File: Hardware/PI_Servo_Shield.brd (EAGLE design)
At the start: 65 x 30 mm, 89 parts, among them J1 RASPBERRYPI-40-PIN-GPIO, J19 QWIIC, J20 USB C, J21 Serial, U1 PCA9685, U2 PCA9306, U3 CH340C

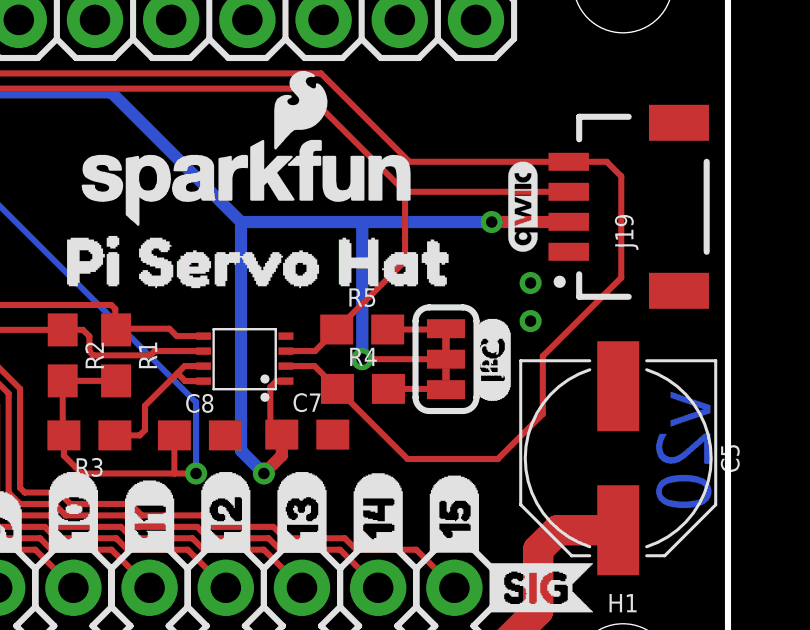
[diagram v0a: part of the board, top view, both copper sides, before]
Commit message: adjusted I2C pullup and label
modified sch note for bypass fuse jumper
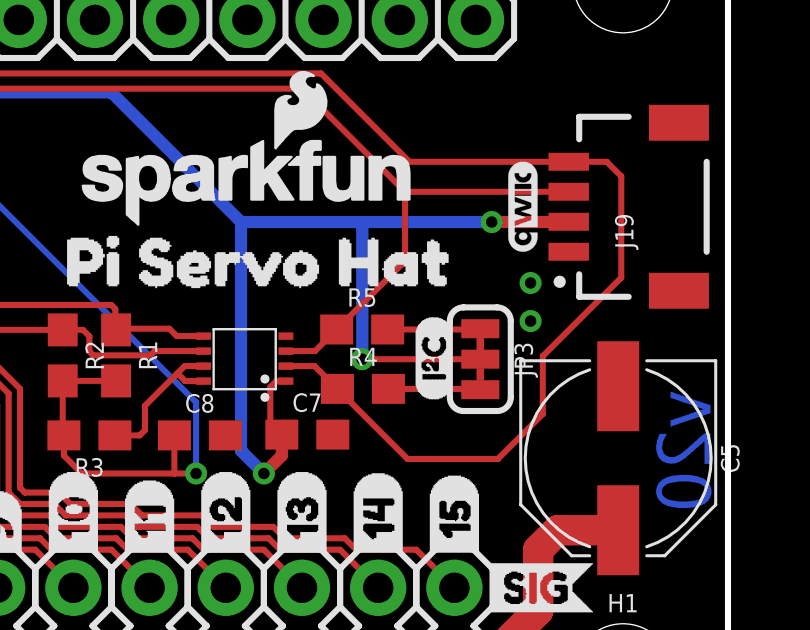
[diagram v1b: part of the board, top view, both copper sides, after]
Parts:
- moved U$2 1.96 mm to (55.2, 12.6)
- moved JP3 1.14 mm to (56.7, 14.0)
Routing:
- net N$2: track 1.93 -> 3.07 mm
- net 3.3VB: track 53.8 -> 54.9 mm
- net N$5: track 1.95 -> 3.10 mm
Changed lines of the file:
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@@
 <layer number="23" name="tOrigins" color="15" fill="1" visible="yes" active="yes"/>
 <layer number="24" name="bOrigins" color="15" fill="1" visible="yes" active="yes"/>
-<layer number="25" name="tNames" color="7" fill="1" visible="yes" active="yes"/>
-<layer number="26" name="bNames" color="7" fill="1" visible="yes" active="yes"/>
-<layer number="27" name="tValues" color="7" fill="1" visible="yes" active="yes"/>
-<layer number="28" name="bValues" color="7" fill="1" visible="yes" active="yes"/>
-<layer number="29" name="tStop" color="7" fill="3" visible="yes" active="yes"/>
-<layer number="30" name="bStop" color="7" fill="6" visible="yes" active="yes"/>
-<layer number="31" name="tCream" color="7" fill="4" visible="yes" active="yes"/>
-<layer number="32" name="bCream" color="7" fill="5" visible="yes" active="yes"/>
-<layer number="33" name="tFinish" color="6" fill="3" visible="yes" active="yes"/>
-<layer number="34" name="bFinish" color="6" fill="6" visible="yes" active="yes"/>
-<layer number="35" name="tGlue" color="7" fill="4" visible="yes" active="yes"/>
-<layer number="36" name="bGlue" color="7" fill="5" visible="yes" active="yes"/>
-<layer number="37" name="tTest" color="7" fill="1" visible="yes" active="yes"/>
-<layer number="38" name="bTest" color="7" fill="1" visible="yes" active="yes"/>
-<layer number="39" name="tKeepout" color="4" fill="11" visible="yes" active="yes"/>
-<layer number="40" name="bKeepout" color="1" fill="11" visible="yes" active="yes"/>
-<layer number="41" name="tRestrict" color="4" fill="10" visible="yes" active="yes"/>
-<layer number="42" name="bRestrict" color="1" fill="10" visible="yes" active="yes"/>
-<layer number="43" name="vRestrict" color="2" fill="10" visible="yes" active="yes"/>
-<layer number="44" name="Drills" color="7" fill="1" visible="yes" active="yes"/>
+<layer number="25" name="tNames" color="7" fill="1" visible="no" active="yes"/>
+<layer number="26" name="bNames" color="7" fill="1" visible="no" active="yes"/>
+<layer number="27" name="tValues" color="7" fill="1" visible="no" active="yes"/>
+<layer number="28" name="bValues" color="7" fill="1" visible="no" active="yes"/>
+<layer number="29" name="tStop" color="7" fill="3" visible="no" active="yes"/>
+<layer number="30" name="bStop" color="7" fill="6" visible="no" active="yes"/>
+<layer number="31" name="tCream" color="7" fill="4" visible="no" active="yes"/>
+<layer number="32" name="bCream" color="7" fill="5" visible="no" active="yes"/>
+<layer number="33" name="tFinish" color="6" fill="3" visible="no" active="yes"/>
+<layer number="34" name="bFinish" color="6" fill="6" visible="no" active="yes"/>
+<layer number="35" name="tGlue" color="7" fill="4" visible="no" active="yes"/>
+<layer number="36" name="bGlue" color="7" fill="5" visible="no" active="yes"/>
+<layer number="37" name="tTest" color="7" fill="1" visible="no" active="yes"/>
+<layer number="38" name="bTest" color="7" fill="1" visible="no" active="yes"/>
+<layer number="39" name="tKeepout" color="4" fill="11" visible="no" active="yes"/>
+<layer number="40" name="bKeepout" color="1" fill="11" visible="no" active="yes"/>
+<layer number="41" name="tRestrict" color="4" fill="10" visible="no" active="yes"/>
+<layer number="42" name="bRestrict" color="1" fill="10" visible="no" active="yes"/>
+<layer number="43" name="vRestrict" color="2" fill="10" visible="no" active="yes"/>
+<layer number="44" name="Drills" color="7" fill="1" visible="no" active="yes"/>
 <layer number="45" name="Holes" color="7" fill="1" visible="yes" active="yes"/>
-<layer number="46" name="Milling" color="3" fill="1" visible="yes" active="yes"/>
-<layer number="47" name="Measures" color="7" fill="1" visible="yes" active="yes"/>
-<layer number="48" name="Document" color="7" fill="1" visible="yes" active="yes"/>
+<layer number="46" name="Milling" color="3" fill="1" visible="no" active="yes"/>
+<layer number="47" name="Measures" color="7" fill="1" visible="no" active="yes"/>
+<layer number="48" name="Document" color="7" fill="1" visible="no" active="yes"/>
 <layer number="49" name="Reference" color="7" fill="1" visible="yes" active="yes"/>
-<layer number="50" name="dxf" color="7" fill="1" visible="yes" active="yes"/>
+<layer number="50" name="dxf" color="7" fill="1" visible="no" active="yes"/>
 <layer number="51" name="tDocu" color="6" fill="1" visible="yes" active="yes"/>
-<layer number="52" name="bDocu" color="7" fill="1" visible="yes" active="yes"/>
+<layer number="52" name="bDocu" color="7" fill="1" visible="no" active="yes"/>
 <layer number="91" name="Nets" color="2" fill="1" visible="no" active="no"/>
 <layer number="92" name="Busses" color="1" fill="1" visible="no" active="no"/>
@@
 <layer number="115" name="ReferenceISLANDS" color="7" fill="1" visible="no" active="no"/>
 <layer number="116" name="Patch_BOT" color="9" fill="4" visible="no" active="no"/>
-<layer number="117" name="PM_Ref" color="7" fill="1" visible="yes" active="yes"/>
+<layer number="117" name="PM_Ref" color="7" fill="1" visible="no" active="yes"/>
 <layer number="118" name="Rect_Pads" color="7" fill="1" visible="no" active="no"/>
-<layer number="119" name="PF_Ref" color="7" fill="1" visible="yes" active="yes"/>
-<layer number="120" name="WFL_Ref" color="7" fill="1" visible="yes" active="yes"/>
+<layer number="119" name="PF_Ref" color="7" fill="1" visible="no" active="yes"/>
+<layer number="120" name="WFL_Ref" color="7" fill="1" visible="no" active="yes"/>
 <layer number="121" name="_tsilk" color="7" fill="1" visible="no" active="no"/>
 <layer number="122" name="_bsilk" color="7" fill="1" visible="no" active="no"/>
@@
 <attribute name="VALUE" x="9.8298" y="2.3622" size="0.6096" layer="27" font="vector" ratio="20" align="top-center"/>
 </element>
-<element name="JP3" library="SparkFun-Jumpers" package="SMT-JUMPER_3_2-NC_TRACE_SILK" value="I2C" x="55.6006" y="13.97" smashed="yes" rot="R270">
-<attribute name="NAME" x="56.7436" y="13.97" size="0.6096" layer="25" font="vector" ratio="20" rot="R270" align="bottom-center"/>
-<attribute name="VALUE" x="54.4576" y="13.97" size="0.6096" layer="27" font="vector" ratio="20" rot="R270" align="top-center"/>
-</element>
-<element name="U$2" library="Qwiic RFID - IDXXLA" package="I_SUPER2_C-()-03" value="" x="57.15" y="12.5222" smashed="yes" rot="R90"/>
+<element name="JP3" library="SparkFun-Jumpers" package="SMT-JUMPER_3_2-NC_TRACE_SILK" value="I2C" x="56.7436" y="13.97" smashed="yes" rot="R270">
+<attribute name="NAME" x="57.8866" y="13.97" size="0.6096" layer="25" font="vector" ratio="20" rot="R270" align="bottom-center"/>
+<attribute name="VALUE" x="55.6006" y="13.97" size="0.6096" layer="27" font="vector" ratio="20" rot="R270" align="top-center"/>
+</element>
+<element name="U$2" library="Qwiic RFID - IDXXLA" package="I_SUPER2_C-()-03" value="" x="55.1942" y="12.573" smashed="yes" rot="R90"/>
 <element name="U$3" library="buzzard_labels" package="028" value="" x="17.78" y="7.0485" smashed="yes" rot="R90"/>
 <element name="U$4" library="buzzard_labels" package="129" value="" x="20.32" y="7.0485" smashed="yes" rot="R90"/>
@@
 <wire x1="48.768" y1="18.542" x2="52.8066" y2="18.542" width="0.4064" layer="16"/>
 <via x="49.53" y="10.16" extent="1-16" drill="0.381"/>
-<wire x1="53.34" y1="18.542" x2="57.1246" y2="18.542" width="0.4064" layer="16"/>
+<wire x1="52.8066" y1="18.542" x2="57.1246" y2="18.542" width="0.4064" layer="16"/>
 <wire x1="49.53" y1="10.16" x2="48.768" y2="10.922" width="0.4064" layer="16"/>
 <wire x1="48.768" y1="10.922" x2="48.768" y2="18.542" width="0.4064" layer="16"/>
@@
 <wire x1="50.1278" y1="11.4554" x2="50.1278" y2="10.7578" width="0.4064" layer="1"/>
 <wire x1="50.1278" y1="10.7578" x2="49.53" y2="10.16" width="0.4064" layer="1"/>
-<wire x1="55.6006" y1="13.97" x2="52.8066" y2="13.97" width="0.2032" layer="1"/>
+<wire x1="56.7436" y1="13.97" x2="52.8066" y2="13.97" width="0.2032" layer="1"/>
 <wire x1="52.8066" y1="13.97" x2="52.8066" y2="18.542" width="0.4064" layer="16"/>
-<wire x1="52.8066" y1="18.542" x2="53.34" y2="18.542" width="0.4064" layer="16"/>
 </signal>
 <signal name="VBUS" class="1">
@@
 <contactref element="JP3" pad="3"/>
 <contactref element="R4" pad="2"/>
-<wire x1="53.682" y1="12.9794" x2="55.5752" y2="12.9794" width="0.2032" layer="1"/>
-<wire x1="55.5752" y1="12.9794" x2="55.6006" y2="12.954" width="0.2032" layer="1"/>
+<wire x1="53.682" y1="12.9794" x2="56.7182" y2="12.9794" width="0.2032" layer="1"/>
+<wire x1="56.7182" y1="12.9794" x2="56.7436" y2="12.954" width="0.2032" layer="1"/>
 </signal>
 <signal name="N$5">
 <contactref element="R5" pad="2"/>
 <contactref element="JP3" pad="1"/>
-<wire x1="53.6566" y1="14.9606" x2="55.5752" y2="14.9606" width="0.2032" layer="1"/>
-<wire x1="55.5752" y1="14.9606" x2="55.6006" y2="14.986" width="0.2032" layer="1"/>
+<wire x1="53.6566" y1="14.9606" x2="56.7182" y2="14.9606" width="0.2032" layer="1"/>
+<wire x1="56.7182" y1="14.9606" x2="56.7436" y2="14.986" width="0.2032" layer="1"/>
 </signal>
 </signals>

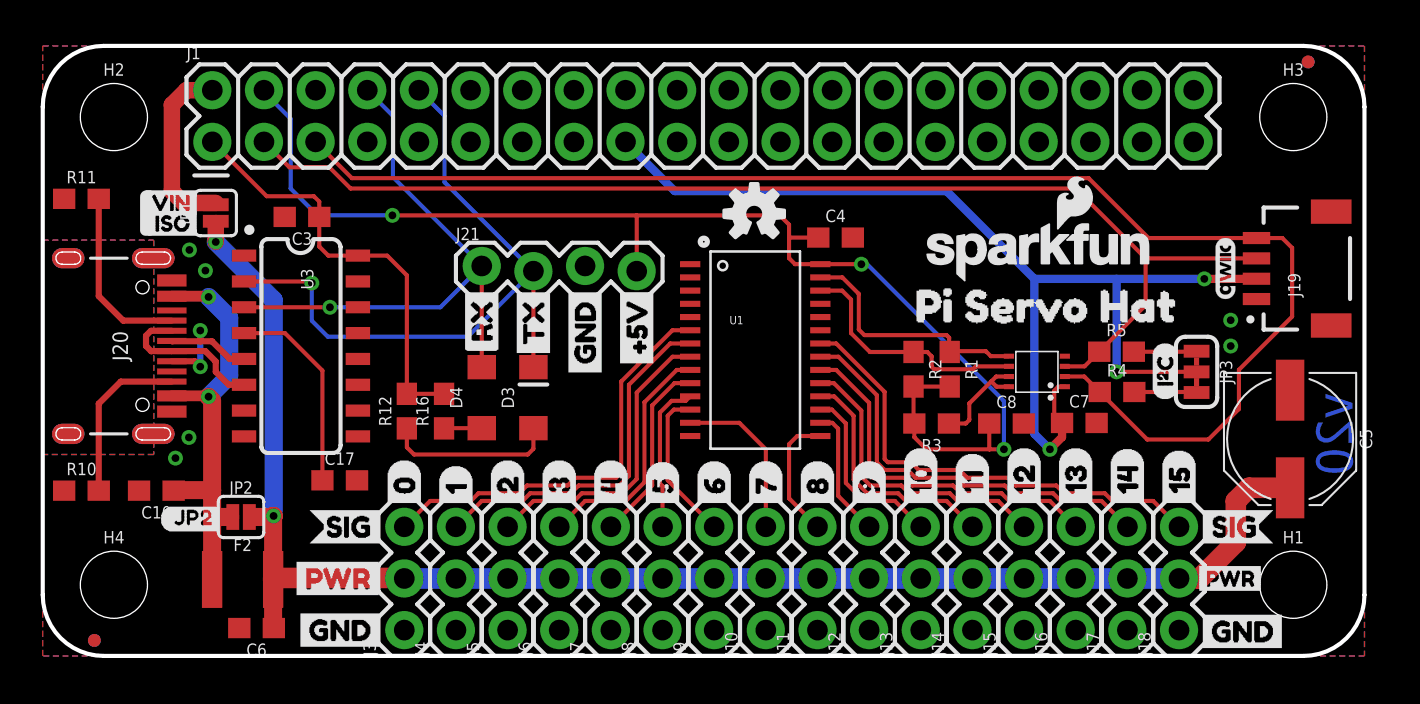
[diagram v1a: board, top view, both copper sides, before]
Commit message: post proto-design-review
SCH cleanup:
-3.3VA and 3.3VB combined into a single net and changed to arrow power symbol
-5VA and 5VB combined into a single net and changed to arrow power symbol
-added note about serial connector mating with sphero RVR
-version to v11, will jump to v20 when going to reds

BRD:
-VIN ISO juper to trace closed.
-Product Name silk updated to include "V2"
-changed "PWR" servo rail labels to "5V"
-corrected RX/TX swap, updated silk to RXI and TXO
-JP2 label changed to "FUSE BP"
-Increased 5V trace to 35 mils on connection from RVR serial header to Pi 5V pins.
-changed version in copper to v11
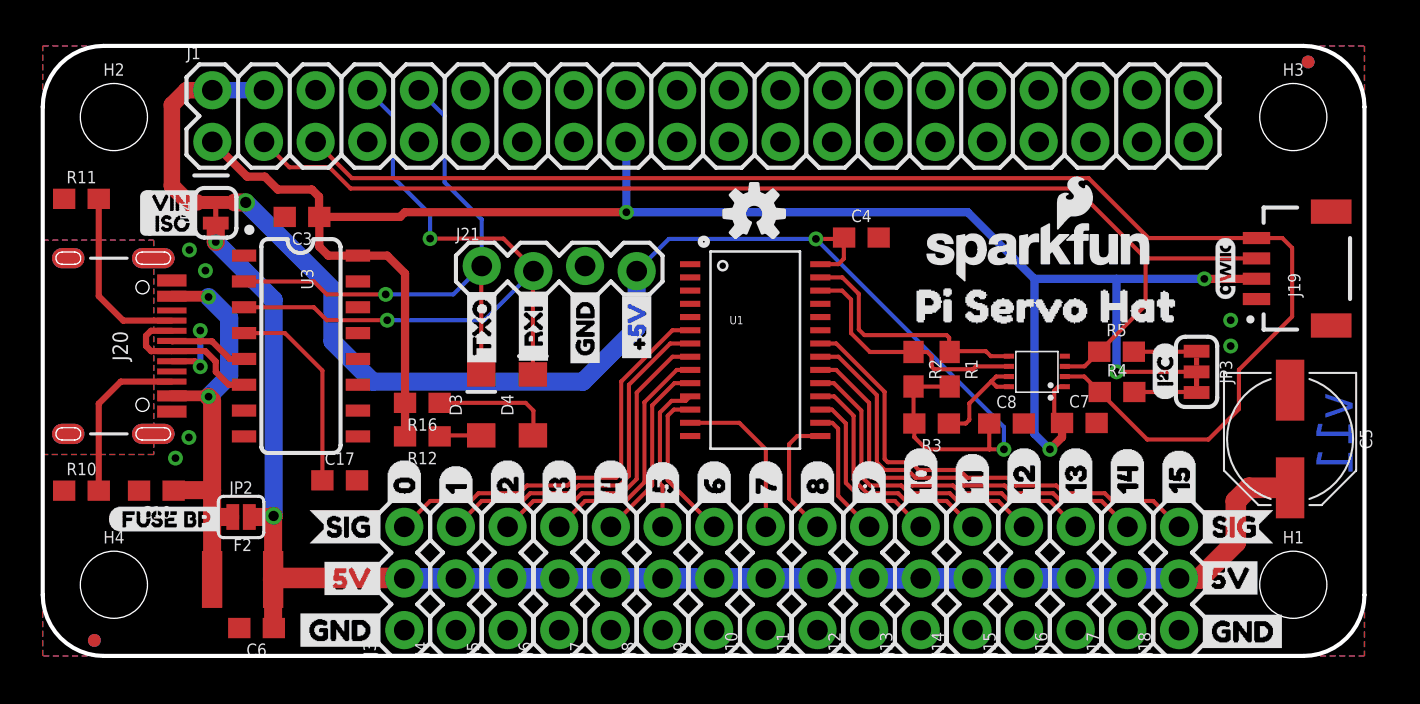
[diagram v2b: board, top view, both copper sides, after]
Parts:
- removed JP1: VIN ISO, SparkFun-Jumpers:SMT-JUMPER_2_NC_PASTE_SILK
- removed U$29: (no value), buzzard_labels:RX23
- added JP4: VIN ISO, SparkFun-Jumpers:SMT-JUMPER_2_NC_TRACE_SILK
- added U$25: (no value), buzzard_labels (8):TXO0
- JP2: value (none) -> FUSE BP
- U$20: device buzzard_labels:PWR1 -> buzzard_labels (6):5V5
- U$24: device buzzard_labels2:PWR0 -> buzzard_labels (6):5V5
- U$27: device buzzard_labels:#5V26 -> buzzard_labels (8):#5V3
- U$28: device buzzard_labels:GND25 -> buzzard_labels (8):GND2
- U$30: device buzzard_labels:TX24 -> buzzard_labels (5):FUSE_BP5
- U$33: device buzzard_labels (4):JP20 -> buzzard_labels (9):_RXI_0
- moved U$30 22.3 mm to (3.17, 6.73), turned to 0 degrees
- moved U$33 19.8 mm to (24.1, 14.1), turned to 90 degrees
- moved D3 2.59 mm to (21.6, 12.3)
- moved D4 2.54 mm to (24.1, 12.3)
- moved R12 1.46 mm to (18.7, 10.8), turned to 180 degrees
- moved U$20 1.33 mm to (13.3, 3.81)
- moved C4 1.27 mm to (40.3, 20.6)
- moved R16 1.14 mm to (18.7, 12.4), turned to 180 degrees
- moved U$28 0.51 mm to (26.7, 14.0)
- moved U$27 0.32 mm to (29.2, 14.2)
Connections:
- removed net 3.3VA: C3.1, J1.1, R12.2, R16.2, U3.16
- removed net 3.3VB: C7.1, J1.17, J19.2, JP3.2, U2.1
- removed net 5VA: J1.2, JP1.2
- removed net 5VB: C4.1, C8.1, J1.4, J21.4, R1.2, R2.2, R3.2, U1.28
- new net 3.3V: C3.1, C7.1, J1.1, J1.17, J19.2, JP3.2, R12.2, R16.2, U2.1, U3.16
- new net 5V: C4.1, C8.1, J1.2, J1.4, J21.4, JP4.2, R1.2, R2.2, R3.2, U1.28
- net RXI: now also J21.2; no longer J21.1
- net TXO: now also J21.1; no longer J21.2
- net VIN: now also JP4.1; no longer JP1.1
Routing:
- net 3.3V: track 0.00 -> 93.7 mm, vias 0 -> 4
- net 5V: track 0.00 -> 78.8 mm, vias 0 -> 3
- net 5VB: track 62.5 -> 0.00 mm, vias 3 -> 0
- net 3.3VB: track 54.9 -> 0.00 mm, vias 3 -> 0
- net 3.3VA: track 21.2 -> 0.00 mm
- net 5VA: track 9.04 -> 0.00 mm
- net RXI: track 28.5 -> 35.1 mm, vias 1 -> 2
- net N$13: track 8.43 -> 2.07 mm
- net TXO: track 33.7 -> 27.8 mm
- net N$12: track 1.86 -> 6.00 mm
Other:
- board text added: "v11"
- board text removed: "v20"

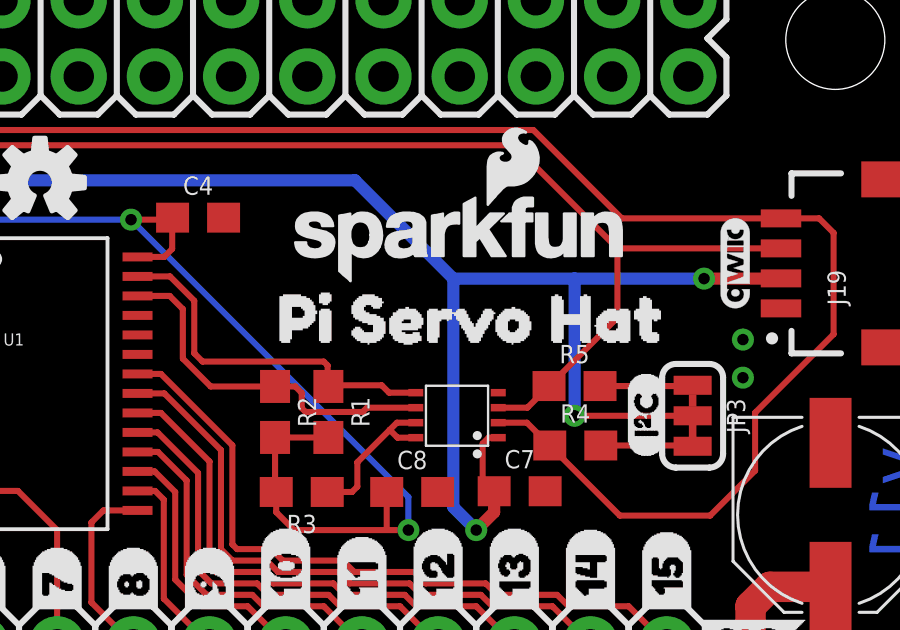
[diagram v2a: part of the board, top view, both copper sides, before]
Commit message: Updated name silk label to include "V2"
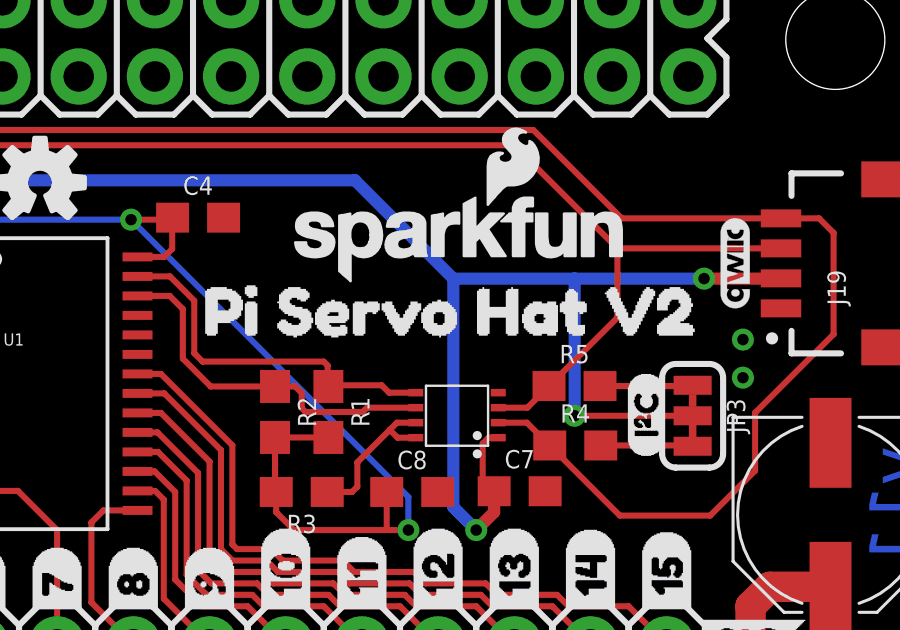
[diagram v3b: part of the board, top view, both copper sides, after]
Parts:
- removed U$26: (no value), buzzard_labels (1):PI_SERVO_HAT0
- added U$29: (no value), buzzard_labels (10):PI_SERVO_HAT_V21
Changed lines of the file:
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@@
 <element name="U$22" library="buzzard_labels" package="SIG3" value="" x="56.5785" y="6.35" smashed="yes"/>
 <element name="U$23" library="buzzard_labels" package="GND25" value="" x="56.5785" y="1.2065" smashed="yes"/>
-<element name="U$26" library="buzzard_labels (1)" package="PI_SERVO_HAT0" value="" x="41.529" y="17.2085" smashed="yes"/>
 <element name="U$31" library="buzzard_labels (3)" package="VIN0" value="" x="4.6736" y="22.2885" smashed="yes"/>
 <element name="U$32" library="buzzard_labels (3)" package="ISO1" value="" x="4.826" y="21.2725" smashed="yes"/>
@@
 <attribute name="VALUE" x="9.652" y="21.7932" size="0.6096" layer="27" font="vector" ratio="20" rot="R90" align="top-center"/>
 </element>
+<element name="U$29" library="buzzard_labels (10)" package="PI_SERVO_HAT_V21" value="" x="39.116" y="17.4498" smashed="yes"/>
 </elements>
 <signals>
